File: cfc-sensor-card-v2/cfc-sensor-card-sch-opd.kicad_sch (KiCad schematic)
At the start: 73 parts, among them Q1 DMP2240UDM, Q2 PMV45EN, Q3 DMP3050LVT-7, Q4 DMP3050LVT-7, Q5 PMV45EN, U2 MAX7310ATE+, U3 MIC842LYC5, U4 MIC842LYC5, U5 MAX4211FETE

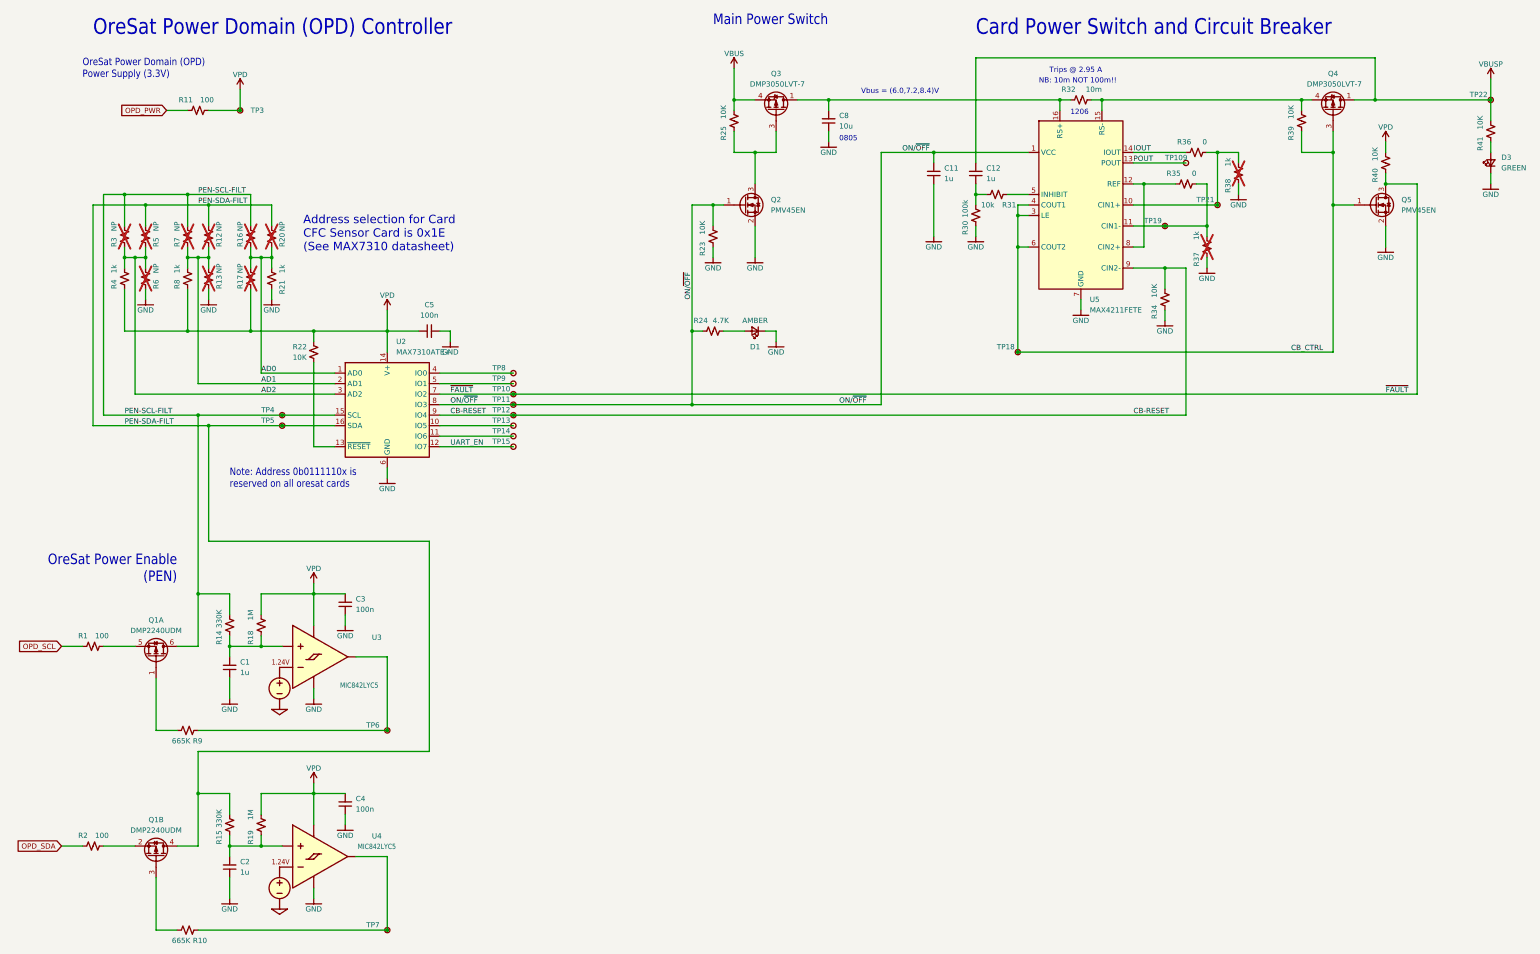
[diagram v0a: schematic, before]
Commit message: Schematic Changes
Made schematic into hierarchy view. Revised OPD to match modern OPD. Removed connectors page. Separated power sequencing and PIRT sensor into 2 pages.
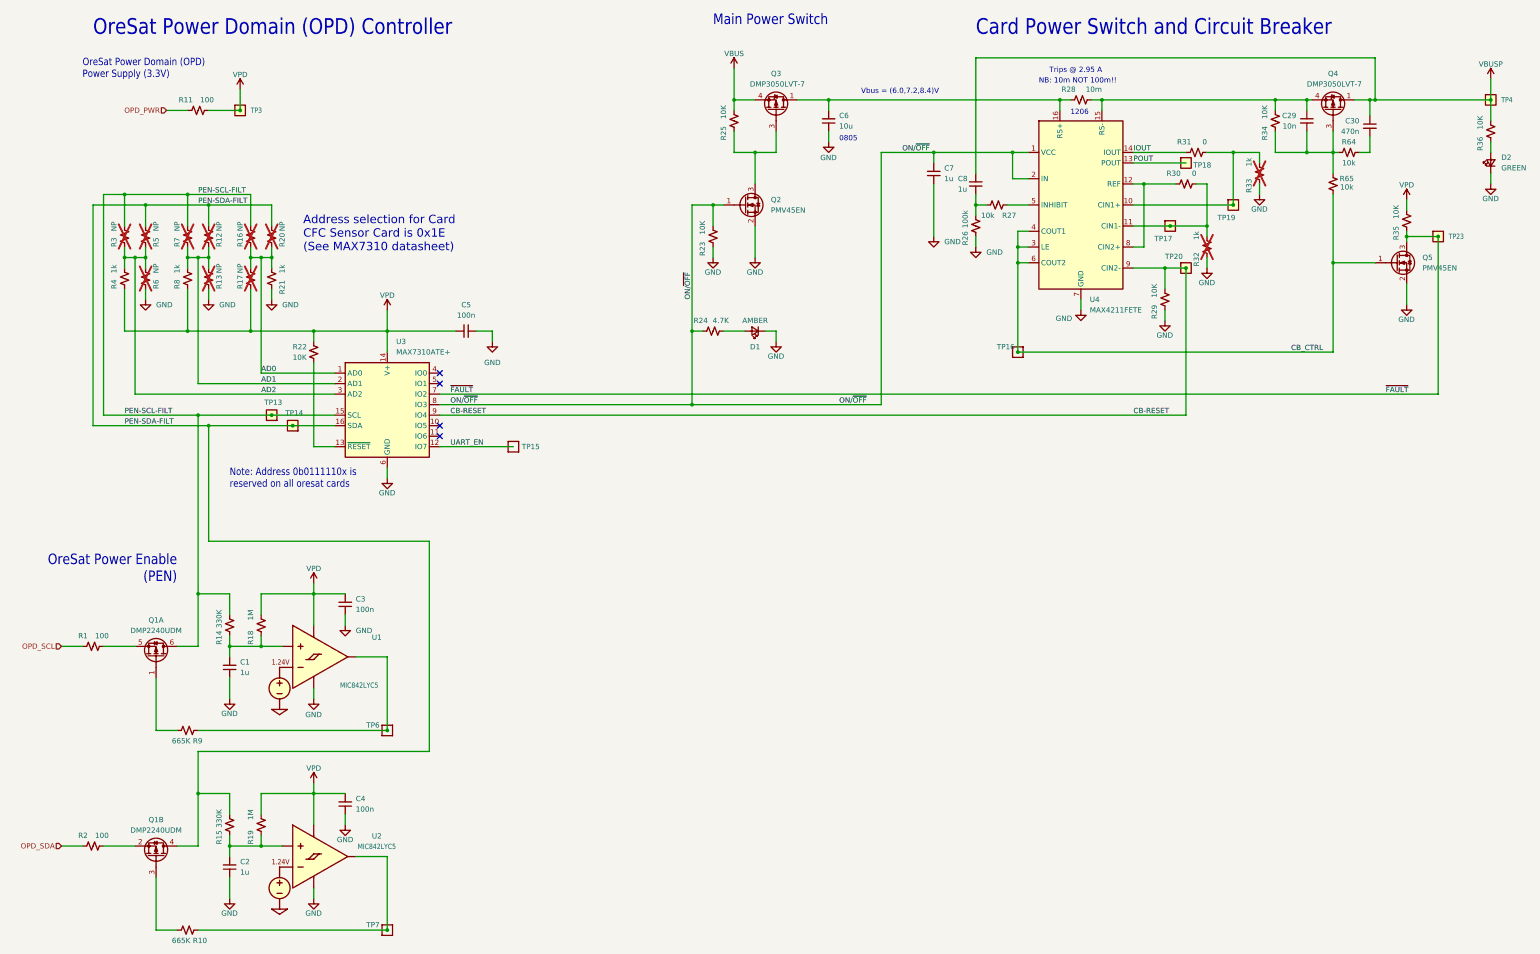
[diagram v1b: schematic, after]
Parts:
- removed TP10, TP109, TP11, TP12, TP13, TP14, TP19, TP21, TP22, TP3, TP4, TP5, TP8, TP9: TestPoint-MinTH, oresat-misc:TestPoint-MinTH, symbol oresat-misc:TestPoint-MinTH
- added C29: 10n, oresat-passives:0603-C-NOSILK, symbol Device:C_Small
- added C30: 470n, oresat-passives:0603-C-NOSILK, symbol Device:C_Small
- added R64, R65: 10k, oresat-passives:0603-C-NOSILK, symbol Device:R_Small_US
- added TP13, TP14, TP17, TP18, TP19, TP20: TEST-POINT, star-tracker-card:2MM-TEST-POINT, symbol star-tracker-card-eagle-import:TEST-POINT
- added TP23, TP3, TP4: Test-Point, oresat-misc:TestPoint-0.75mm-th, symbol Oresat Misc:Test-Point-0.75mm-th
- TP15, TP6, TP7: footprint oresat-misc:TestPoint-MinTH -> oresat-misc:TestPoint_Pad_D1.0mm; symbol oresat-misc:TestPoint-MinTH -> Oresat Misc:Test-Point-1mm-round
- TP16: renamed from TP18; footprint oresat-misc:TestPoint-MinTH -> oresat-misc:TestPoint_Pad_D1.0mm; symbol oresat-misc:TestPoint-MinTH -> Oresat Misc:Test-Point-1mm-round
- U4: renamed from U5; symbol oresat-ics:MAX4211FETE -> oresat-ics:MAX4211D/E/F
- renumbered C8 to C6, C11 to C7, C12 to C8, D3 to D2, R30 to R26, R31 to R27, R32 to R28, R34 to R29, R35 to R30, R36 to R31, R37 to R32, R38 to R33, R39 to R34, R40 to R35, R41 to R36, U3 to U1, U4 to U2, U2 to U3
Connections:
- net CB-RESET: now also TP20.1
- net CB_CTRL: now also R65.2; no longer Q4.3 (G), R34.1
- net ON/~{OFF}: now also U4.2 (IN)
- net PEN-SCL-FILT: now also TP13.1
- net PEN-SDA-FILT: now also TP14.1
- net POUT: now also TP18.1
- net VBUSP: now also C30.1, TP4.1
- net VPD: now also TP3.1
- net ~{FAULT}: now also TP23.1
- net at R31.2, R33.2, U4.10 (CIN1+): now also TP19.1
- net at R30.2, R32.2, U4.11 (CIN1-): now also TP17.1
- net at Q4.4 (S), R28.2, R34.2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: now also C29.1
- new net: C30.2, R64.2
- new net: C29.2, Q4.3 (G), R34.1, R64.1, R65.1
- no-connect marks 0 -> 4
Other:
- moved on the sheet: C8, Q5, R26, R27, R33, R34, R35

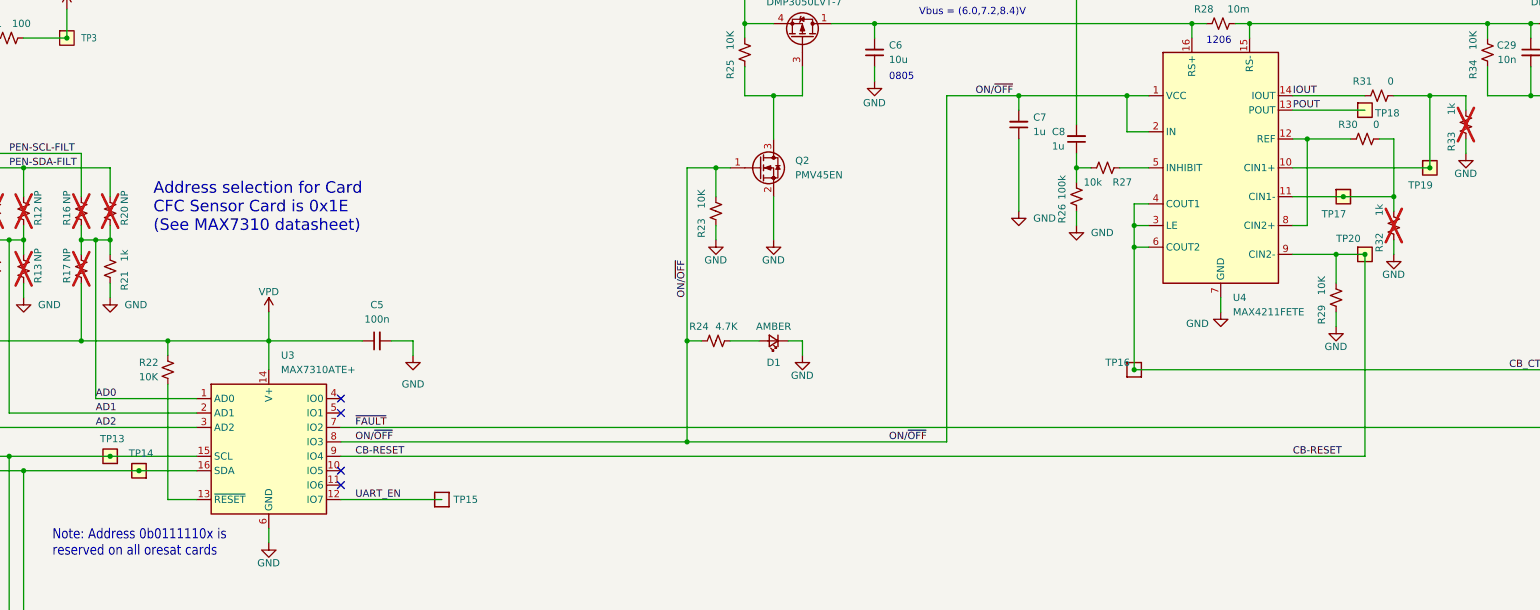
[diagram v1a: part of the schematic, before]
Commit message: Update
Fixed a couple of library issues on testpoints and other misc components. Added Pull up resistors to 8 channel i2c ic
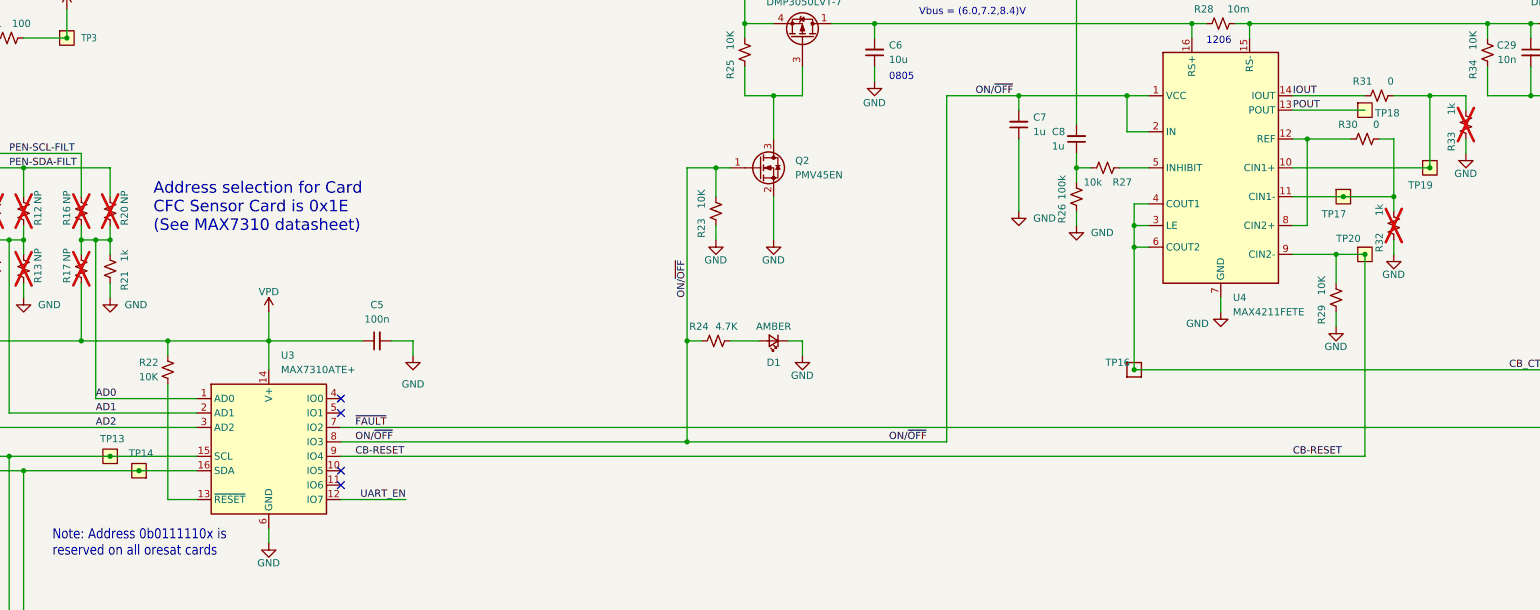
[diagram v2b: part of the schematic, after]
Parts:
- removed TP15: TestPoint-MinTH, oresat-misc:TestPoint_Pad_D1.0mm, symbol Oresat Misc:Test-Point-1mm-round
- TP13, TP14, TP17, TP18, TP19, TP20: footprint star-tracker-card:2MM-TEST-POINT -> oresat-misc:TestPoint-0.75mm-th; symbol star-tracker-card-eagle-import:TEST-POINT -> oresat-misc:Test-Point-0.75mm-th
- TP16, TP6, TP7: symbol Oresat Misc:Test-Point-1mm-round -> oresat-misc:Test-Point-1mm-round
- TP23, TP3, TP4: symbol Oresat Misc:Test-Point-0.75mm-th -> oresat-misc:Test-Point-0.75mm-th
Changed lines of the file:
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@@
 	(wire
 		(pts
-			(xy 121.92 127) (xy 139.7 127)
+			(xy 121.92 127) (xy 133.35 127)
 		)
 		(stroke
@@
 	)
 	(label "UART_EN"
-		(at 124.46 127 0)
+		(at 133.35 127 180)
 		(effects
 			(font
 				(size 1.27 1.27)
 			)
-			(justify left bottom)
+			(justify right bottom)
 		)
 	)
@@
 	)
 	(symbol
-		(lib_id "Oresat Misc:Test-Point-1mm-round")
-		(at 139.7 127 0)
-		(unit 1)
-		(body_style 1)
-		(exclude_from_sim no)
-		(in_bom no)
-		(on_board yes)
-		(in_pos_files yes)
-		(dnp no)
-		(property "Reference" "TP15"
-			(at 141.732 127 0)
-			(show_name no)
-			(do_not_autoplace no)
-			(effects
-				(font
-					(size 1.27 1.27)
-				)
-				(justify left)
-			)
-		)
-		(property "Value" "TestPoint-MinTH"
-			(at 139.7 120.015 0)
-			(hide yes)
-			(show_name no)
-			(do_not_autoplace no)
-			(effects
-				(font
-					(size 1.27 1.27)
-				)
-			)
-		)
-		(property "Footprint" "oresat-misc:TestPoint_Pad_D1.0mm"
-			(at 139.7 116.84 0)
-			(hide yes)
-			(show_name no)
-			(do_not_autoplace no)
-			(effects
-				(font
-					(size 1.27 1.27)
-				)
-			)
-		)
-		(property "Datasheet" ""
-			(at 139.7 127 0)
-			(hide yes)
-			(show_name no)
-			(do_not_autoplace no)
-			(effects
-				(font
-					(size 1.27 1.27)
-				)
-			)
-		)
-		(property "Description" "1mm round SMT test point"
-			(at 139.7 127 0)
-			(hide yes)
-			(show_name no)
-			(do_not_autoplace no)
-			(effects
-				(font
-					(size 1.27 1.27)
-				)
-			)
-		)
-		(property "DIS" ""
-			(at 139.7 127 0)
-			(hide yes)
-			(show_name no)
-			(do_not_autoplace no)
-			(effects
-				(font
-					(size 1.27 1.27)
-				)
-			)
-		)
-		(pin "1"
-		)
-		(instances
-			(project "cfc-sensor-card"
-				(path "/8c53300c-27d6-4efc-b05b-8b907d6da3f5/32b02a49-e716-4e99-9e51-c04d4b68afa0"
-					(reference "TP15")
-					(unit 1)
-				)
-			)
-		)
-	)
-	(symbol
 		(lib_id "oresat-power:VPD")
 		(at 91.44 208.28 0)
@@
 	)
 	(symbol
-		(lib_id "Oresat Misc:Test-Point-1mm-round")
+		(lib_id "oresat-misc:Test-Point-1mm-round")
 		(at 109.22 243.84 0)
 		(unit 1)
@@
 	)
 	(symbol
-		(lib_id "star-tracker-card-eagle-import:TEST-POINT")
+		(lib_id "oresat-misc:Test-Point-0.75mm-th")
 		(at 86.36 121.92 180)
 		(unit 1)
@@
 			)
 		)
-		(property "Footprint" "star-tracker-card:2MM-TEST-POINT"
-			(at 86.36 121.92 0)
+		(property "Footprint" "oresat-misc:TestPoint-0.75mm-th"
+			(at 86.36 132.08 0)
 			(hide yes)
 			(show_name no)
@@
 			)
 		)
-		(property "Description" ""
+		(property "Description" "0.75 mm TH test point; good for scope probes and jumpers"
 			(at 86.36 121.92 0)
 			(hide yes)
@@
 			)
 		)
-		(property "Description" "Green 520nm LED Indication - Discrete 3.2V 0603 (1608 Metric) - 430 mcd @ 20 mA"
+		(property "Description" "Light emitting diode, small symbol"
 			(at 375.92 58.42 0)
 			(hide yes)
@@
 			)
 		)
+		(property "Sim.Pins" "1=K 2=A"
+			(at 375.92 58.42 0)
+			(hide yes)
+			(show_name no)
+			(do_not_autoplace no)
+			(effects
+				(font
+					(size 1.27 1.27)
+				)
+			)
+		)
 		(pin "1"
 		)
@@
 	)
 	(symbol
-		(lib_id "star-tracker-card-eagle-import:TEST-POINT")
+		(lib_id "oresat-misc:Test-Point-0.75mm-th")
 		(at 302.26 83.82 0)
 		(unit 1)
@@
 			)
 		)
-		(property "Footprint" "star-tracker-card:2MM-TEST-POINT"
-			(at 302.26 83.82 0)
+		(property "Footprint" "oresat-misc:TestPoint-0.75mm-th"
+			(at 302.26 73.66 0)
 			(hide yes)
 			(show_name no)
@@
 			)
 		)
-		(property "Description" ""
+		(property "Description" "0.75 mm TH test point; good for scope probes and jumpers"
 			(at 302.26 83.82 0)
 			(hide yes)
@@
 	)
 	(symbol
-		(lib_id "Oresat Misc:Test-Point-0.75mm-th")
+		(lib_id "oresat-misc:Test-Point-0.75mm-th")
 		(at 363.22 76.2 0)
 		(unit 1)
@@
 	)
 	(symbol
-		(lib_id "Oresat Misc:Test-Point-0.75mm-th")
+		(lib_id "oresat-misc:Test-Point-0.75mm-th")
 		(at 73.66 45.72 0)
 		(unit 1)
@@
 	)
 	(symbol
-		(lib_id "star-tracker-card-eagle-import:TEST-POINT")
+		(lib_id "oresat-misc:Test-Point-0.75mm-th")
 		(at 302.26 58.42 0)
 		(unit 1)
@@
 			)
 		)
-		(property "Footprint" "star-tracker-card:2MM-TEST-POINT"
-			(at 302.26 58.42 0)
+		(property "Footprint" "oresat-misc:TestPoint-0.75mm-th"
+			(at 302.26 48.26 0)
 			(hide yes)
 			(show_name no)
@@
 			)
 		)
-		(property "Description" ""
+		(property "Description" "0.75 mm TH test point; good for scope probes and jumpers"
 			(at 302.26 58.42 0)
 			(hide yes)
@@
 	)
 	(symbol
-		(lib_id "star-tracker-card-eagle-import:TEST-POINT")
+		(lib_id "oresat-misc:Test-Point-0.75mm-th")
 		(at 298.45 73.66 0)
 		(unit 1)
@@
 			)
 		)
-		(property "Footprint" "star-tracker-card:2MM-TEST-POINT"
-			(at 298.45 73.66 0)
+		(property "Footprint" "oresat-misc:TestPoint-0.75mm-th"
+			(at 298.45 63.5 0)
 			(hide yes)
 			(show_name no)
@@
 			)
 		)
-		(property "Description" ""
+		(property "Description" "0.75 mm TH test point; good for scope probes and jumpers"
 			(at 298.45 73.66 0)
 			(hide yes)
@@
 	)
 	(symbol
-		(lib_id "Oresat Misc:Test-Point-1mm-round")
+		(lib_id "oresat-misc:Test-Point-1mm-round")
 		(at 261.62 104.14 0)
 		(unit 1)
@@
 	)
 	(symbol
-		(lib_id "Oresat Misc:Test-Point-1mm-round")
+		(lib_id "oresat-misc:Test-Point-1mm-round")
 		(at 109.22 195.58 0)
 		(unit 1)
@@
 	)
 	(symbol
-		(lib_id "Oresat Misc:Test-Point-0.75mm-th")
+		(lib_id "oresat-misc:Test-Point-0.75mm-th")
 		(at 375.92 43.18 0)
 		(unit 1)
@@
 	)
 	(symbol
+		(lib_name "LED_Small_1")
 		(lib_id "Device:LED_Small")
 		(at 198.12 99.06 180)
@@
 			)
 		)
-		(property "Description" "Amber 605nm LED Indication - Discrete 2V 0603 (1608 Metric)"
+		(property "Description" "Light emitting diode, small symbol"
 			(at 198.12 99.06 0)
 			(hide yes)
@@
 			)
 		)
+		(property "Sim.Pins" "1=K 2=A"
+			(at 198.12 99.06 0)
+			(hide yes)
+			(show_name no)
+			(do_not_autoplace no)
+			(effects
+				(font
+					(size 1.27 1.27)
+				)
+			)
+		)
 		(pin "1"
 		)
@@
 	)
 	(symbol
-		(lib_id "star-tracker-card-eagle-import:TEST-POINT")
+		(lib_id "oresat-misc:Test-Point-0.75mm-th")
 		(at 81.28 119.38 180)
 		(unit 1)
@@
 			)
 		)
-		(property "Footprint" "star-tracker-card:2MM-TEST-POINT"
-			(at 81.28 119.38 0)
+		(property "Footprint" "oresat-misc:TestPoint-0.75mm-th"
+			(at 81.28 129.54 0)
 			(hide yes)
 			(show_name no)
@@
 			)
 		)
-		(property "Description" ""
+		(property "Description" "0.75 mm TH test point; good for scope probes and jumpers"
 			(at 81.28 119.38 0)
 			(hide yes)
@@
 	)
 	(symbol
-		(lib_id "star-tracker-card-eagle-import:TEST-POINT")
+		(lib_id "oresat-misc:Test-Point-0.75mm-th")
 		(at 313.69 68.58 0)
 		(unit 1)
@@
 			)
 		)
-		(property "Footprint" "star-tracker-card:2MM-TEST-POINT"
-			(at 313.69 68.58 0)
+		(property "Footprint" "oresat-misc:TestPoint-0.75mm-th"
+			(at 313.69 58.42 0)
 			(hide yes)
 			(show_name no)
@@
 			)
 		)
-		(property "Description" ""
+		(property "Description" "0.75 mm TH test point; good for scope probes and jumpers"
 			(at 313.69 68.58 0)
 			(hide yes)
